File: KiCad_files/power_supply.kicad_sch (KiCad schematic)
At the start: 5 parts, among them Q2 DMP3099L, U7 LTC4412xS6

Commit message: power supply
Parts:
- removed C5: C, symbol Device:C
- added C17: 22n, symbol Device:C
- added C18, C19, C20: 0.1u, symbol Device:C
- added C21: 33p, symbol Device:C
- added C5 (x2): 22u, symbol Device:C
- added D3: 1N4148, Diode_THT:D_DO-35_SOD27_P7.62mm_Horizontal, symbol Diode:1N4148
- added L4: 5u, symbol Device:L
- added R10: 100k, symbol Device:R
- added R11: 20, symbol Device:R
- added R12: 5.6k, symbol Device:R
- added R13: 13k, symbol Device:R
- added R14: 40.2k, symbol Device:R
- added R15: 470k, symbol Device:R
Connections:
- net +3.3V: now also C21.2, C5.1, L4.2, R14.2, R15.1; no longer U8.7 (VCC)
- net GND: now also U7.3 (CTL), U8.4 (GND), C17.1, C18.1, C20.1, C5.2, C5.2, R13.1
- net VBUS: no longer U7.6 (SENSE)
- net power_mux: now also R15.2
- net at U8.1 (SS): now also C17.2
- net at D2.1 (K), Q2.2 (S), U8.2 (IN): now also U7.6 (SENSE), C20.2, C5.1, R10.2
- net at U8.3 (SW): now also C19.1, L4.1
- net at U8.5 (BST): now also D3.1 (K), R11.1
- net at U8.6 (EN/SYNC): now also R10.1
- net at U8.8 (BST): now also R12.1
- net +BATT renamed BATT
- new net: C21.1, R12.2, R13.2, R14.1
- new net: C18.2, D3.2 (A), U8.7 (VCC)
- new net: C19.2, R11.2

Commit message: sadfsadf
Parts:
- added C25, C26: 0, symbol Device:C
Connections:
- net +3.3V: now also C25.1
- net GND: now also C25.2, C26.2
- net at C20.2, C5.1, D2.1 (K)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: now also C26.1
- net BATT renamed BAT
- net power_mux renamed BAT_STAT
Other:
- note removed: "To load"
- moved on the sheet: C5

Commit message: mohloilut korjattu
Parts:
- removed C25, C26: 0, symbol Device:C
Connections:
- net BAT renamed BATT
- net BAT_STAT renamed power_mux
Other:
- note added: "To load"
- moved on the sheet: C5

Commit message: hierarkiset pinnit poweriin
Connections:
- net BATT renamed BAT
- net power_mux renamed BAT_STAT
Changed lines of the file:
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@@
+	)
+	(junction
+		(at 254 95.25)
+		(diameter 0)
+		(color 0 0 0 0)
 	)
 	(junction
@@
 	)
 	(junction
-		(at 254 118.11)
-		(diameter 0)
-		(color 0 0 0 0)
-	)
-	(junction
 		(at 152.4 72.39)
 		(diameter 0)
@@
 	)
 	(junction
-		(at 254 95.25)
+		(at 254 118.11)
 		(diameter 0)
 		(color 0 0 0 0)
@@
 	(wire
 		(pts
-			(xy 34.29 72.39) (xy 115.57 72.39)
-		)
-		(stroke
-			(width 0)
-			(type default)
-		)
-	)
-	(wire
-		(pts
 			(xy 241.3 106.68) (xy 241.3 114.3)
 		)
@@
 	(wire
 		(pts
-			(xy 34.29 85.09) (xy 58.42 85.09)
-		)
-		(stroke
-			(width 0)
-			(type default)
-		)
-	)
-	(wire
-		(pts
 			(xy 152.4 63.5) (xy 152.4 72.39)
 		)
@@
 	(wire
 		(pts
+			(xy 254 95.25) (xy 265.43 95.25)
+		)
+		(stroke
+			(width 0)
+			(type default)
+		)
+	)
+	(wire
+		(pts
 			(xy 143.51 72.39) (xy 143.51 81.28)
 		)
@@
 	(wire
 		(pts
+			(xy 109.22 72.39) (xy 115.57 72.39)
+		)
+		(stroke
+			(width 0)
+			(type default)
+		)
+	)
+	(wire
+		(pts
 			(xy 254 78.74) (xy 254 81.28)
 		)
@@
 	(wire
 		(pts
-			(xy 254 95.25) (xy 266.7 95.25)
-		)
-		(stroke
-			(width 0)
-			(type default)
-		)
-	)
-	(wire
-		(pts
 			(xy 161.29 74.93) (xy 161.29 95.25)
 		)
@@
 	(wire
 		(pts
+			(xy 254 118.11) (xy 266.7 118.11)
+		)
+		(stroke
+			(width 0)
+			(type default)
+		)
+	)
+	(wire
+		(pts
 			(xy 161.29 69.85) (xy 170.18 69.85)
 		)
@@
 	(wire
 		(pts
-			(xy 254 118.11) (xy 266.7 118.11)
+			(xy 25.4 85.09) (xy 58.42 85.09)
 		)
 		(stroke
@@
 		)
 	)
-	(global_label "power_mux"
+	(hierarchical_label "BAT"
 		(shape input)
-		(at 266.7 118.11 0)
-		(fields_autoplaced yes)
+		(at 25.4 85.09 180)
 		(effects
 			(font
 				(size 1.27 1.27)
 			)
-			(justify left)
-		)
-		(property "Intersheetrefs" "${INTERSHEET_REFS}"
-			(at 280.0265 118.11 0)
-			(show_name yes)
-			(effects
-				(font
-					(size 1.27 1.27)
-				)
-				(justify left)
-				(hide yes)
-			)
-		)
-	)
-	(global_label "VBUS"
-		(shape input)
-		(at 34.29 72.39 180)
-		(fields_autoplaced yes)
+			(justify right)
+		)
+	)
+	(hierarchical_label "BAT_STAT"
+		(shape output)
+		(at 266.7 118.11 0)
 		(effects
 			(font
 				(size 1.27 1.27)
 			)
-			(justify right)
-		)
-		(property "Intersheetrefs" "${INTERSHEET_REFS}"
-			(at 26.4062 72.39 0)
-			(effects
-				(font
-					(size 1.27 1.27)
-				)
-				(justify right)
-				(hide yes)
-			)
-		)
-	)
-	(global_label "+3.3V"
-		(shape input)
-		(at 266.7 95.25 0)
-		(fields_autoplaced yes)
-		(effects
-			(font
-				(size 1.27 1.27)
-			)
 			(justify left)
-		)
-		(property "Intersheetrefs" "${INTERSHEET_REFS}"
-			(at 275.37 95.25 0)
-			(effects
-				(font
-					(size 1.27 1.27)
-				)
-				(justify left)
-				(hide yes)
-			)
-		)
-	)
-	(global_label "BATT"
-		(shape input)
-		(at 34.29 85.09 180)
-		(fields_autoplaced yes)
-		(effects
-			(font
-				(size 1.27 1.27)
-			)
-			(justify right)
-		)
-		(property "Intersheetrefs" "${INTERSHEET_REFS}"
-			(at 27.011 85.09 0)
-			(effects
-				(font
-					(size 1.27 1.27)
-				)
-				(justify right)
-				(hide yes)
-			)
 		)
 	)
@@
 	)
 	(symbol
+		(lib_id "power:VBUS")
+		(at 109.22 72.39 90)
+		(unit 1)
+		(exclude_from_sim no)
+		(in_bom yes)
+		(on_board yes)
+		(dnp no)
+		(fields_autoplaced yes)
+		(property "Reference" "#PWR021"
+			(at 113.03 72.39 0)
+			(effects
+				(font
+					(size 1.27 1.27)
+				)
+				(hide yes)
+			)
+		)
+		(property "Value" "VBUS"
+			(at 105.41 72.3899 90)
+			(effects
+				(font
+					(size 1.27 1.27)
+				)
+				(justify left)
+			)
+		)
+		(property "Footprint" ""
+			(at 109.22 72.39 0)
+			(effects
+				(font
+					(size 1.27 1.27)
+				)
+				(hide yes)
+			)
+		)
+		(property "Datasheet" ""
+			(at 109.22 72.39 0)
+			(effects
+				(font
+					(size 1.27 1.27)
+				)
+				(hide yes)
+			)
+		)
+		(property "Description" "Power symbol creates a global label with name \"VBUS\""
+			(at 109.22 72.39 0)
+			(effects
+				(font
+					(size 1.27 1.27)
+				)
+				(hide yes)
+			)
+		)
+		(pin "1"
+		)
+		(instances
+			(project ""
+				(path "/186d5500-054c-4b47-a89c-85f6ce2abe33/718dca9f-314d-4628-afec-7956f3606013"
+					(reference "#PWR021")
+					(unit 1)
+				)
+			)
+		)
+	)
+	(symbol
 		(lib_id "Device:R")
 		(at 214.63 69.85 90)
@@
 					(unit 1)
 				)
+			)
+		)
+	)
+	(symbol
+		(lib_id "power:+3.3V")
+		(at 265.43 95.25 270)
+		(unit 1)
+		(exclude_from_sim no)
+		(in_bom yes)
+		(on_board yes)
+		(dnp no)
+		(fields_autoplaced yes)
+		(property "Reference" "#PWR020"
+			(at 261.62 95.25 0)
+			(effects
+				(font
+					(size 1.27 1.27)
+				)
+				(hide yes)
+			)
+		)
+		(property "Value" "+3.3V"
+			(at 269.24 95.2499 90)
+			(effects
+				(font
+					(size 1.27 1.27)
+				)
+				(justify left)
+			)
+		)
+		(property "Footprint" ""
+			(at 265.43 95.25 0)
+			(effects
+				(font
+					(size 1.27 1.27)
+				)
+				(hide yes)
+			)
+		)
+		(property "Datasheet" ""
+			(at 265.43 95.25 0)
+			(effects
+				(font
+					(size 1.27 1.27)
+				)
+				(hide yes)
+			)
+		)
+		(property "Description" "Power symbol creates a global label with name \"+3.3V\""
+			(at 265.43 95.25 0)
+			(effects
+				(font
+					(size 1.27 1.27)
+				)
+				(hide yes)
+			)
+		)
+		(pin "1"
+		)
+		(instances
+			(project ""
+				(path "/186d5500-054c-4b47-a89c-85f6ce2abe33/718dca9f-314d-4628-afec-7956f3606013"
+					(reference "#PWR020")
+					(unit 1)
+				)

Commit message: tekstiä
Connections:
- net BAT renamed BATT
- net BAT_STAT renamed power_mux

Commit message: footprinttejä
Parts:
- added C25, C26: 0, symbol Device:C
- U8: footprint (none) -> Package_TO_SOT_SMD:TSOT-23-8
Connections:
- net +3.3V: now also C25.1
- net GND: now also C25.2, C26.2
- net at C20.2, C5.1, D2.1 (K)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: now also C26.1
- net BATT renamed BAT
- net power_mux renamed BAT_STAT
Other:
- note removed: "To load"
- moved on the sheet: C5

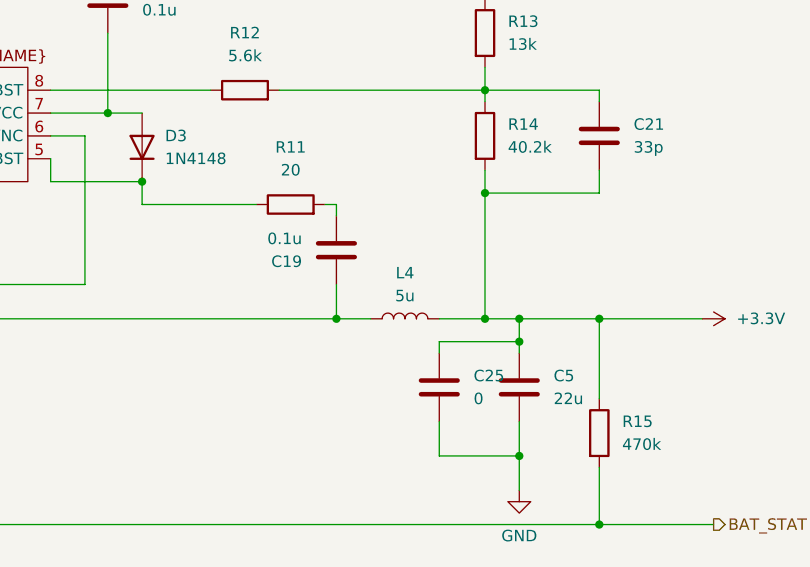
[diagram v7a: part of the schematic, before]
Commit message: footprints for powersupply
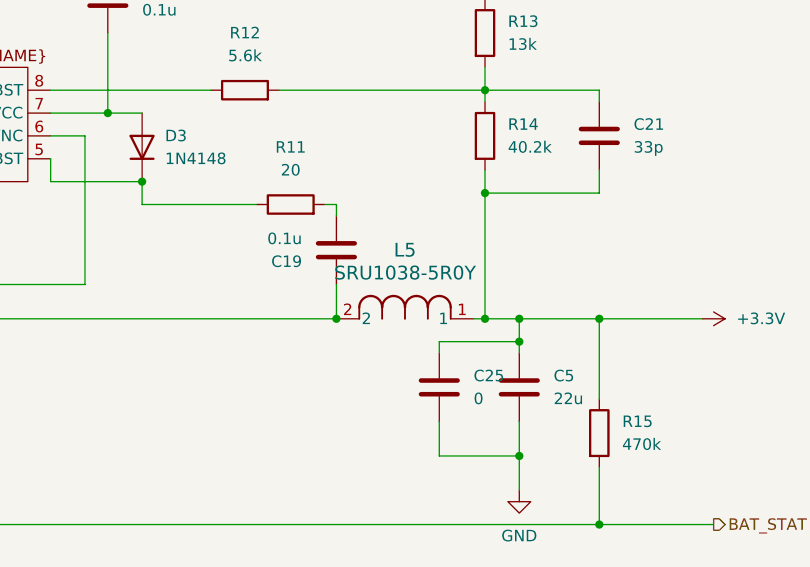
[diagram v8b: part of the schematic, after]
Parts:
- removed L4: 5u, symbol Device:L
- added L5: SRU1038-5R0Y, Inductor_SMD:L_Bourns-SRU1028_10.0x10.0mm, symbol 1_projektin osat:SRU1038-5R0Y
- C17, C18, C19, C20, C21: footprint (none) -> Capacitor_SMD:C_0805_2012Metric_Pad1.18x1.45mm_HandSolder
- C25, C26, C5: footprint (none) -> Capacitor_SMD:C_1206_3216Metric_Pad1.33x1.80mm_HandSolder
- D2: footprint (none) -> Diode_SMD:D_SOD-323_HandSoldering
- D3: footprint Diode_THT:D_DO-35_SOD27_P7.62mm_Horizontal -> Diode_SMD:D_SOD-323F
- R10, R11, R12, R13, R14, R15: footprint (none) -> Resistor_SMD:R_0805_2012Metric_Pad1.20x1.40mm_HandSolder
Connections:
- net +3.3V: now also L5.1
- net at C19.1, U8.3 (SW): now also L5.2
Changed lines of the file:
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@@
+	)
+	(junction
+		(at 142.24 90.17)
+		(diameter 0)
+		(color 0 0 0 0)
 	)
 	(junction
@@
 	)
 	(junction
-		(at 142.24 90.17)
+		(at 245.11 95.25)
+		(diameter 0)
+		(color 0 0 0 0)
+	)
+	(junction
+		(at 125.73 72.39)
+		(diameter 0)
+		(color 0 0 0 0)
+	)
+	(junction
+		(at 142.24 77.47)
+		(diameter 0)
+		(color 0 0 0 0)
+	)
+	(junction
+		(at 152.4 72.39)
+		(diameter 0)
+		(color 0 0 0 0)
+	)
+	(junction
+		(at 241.3 81.28)
+		(diameter 0)
+		(color 0 0 0 0)
+	)
+	(junction
+		(at 80.01 128.27)
+		(diameter 0)
+		(color 0 0 0 0)
+	)
+	(junction
+		(at 241.3 69.85)
+		(diameter 0)
+		(color 0 0 0 0)
+	)
+	(junction
+		(at 245.11 110.49)
 		(diameter 0)
 		(color 0 0 0 0)
@@
 	)
 	(junction
-		(at 245.11 95.25)
-		(diameter 0)
-		(color 0 0 0 0)
-	)
-	(junction
-		(at 125.73 72.39)
-		(diameter 0)
-		(color 0 0 0 0)
-	)
-	(junction
-		(at 142.24 77.47)
-		(diameter 0)
-		(color 0 0 0 0)
-	)
-	(junction
-		(at 152.4 72.39)
-		(diameter 0)
-		(color 0 0 0 0)
-	)
-	(junction
-		(at 241.3 81.28)
-		(diameter 0)
-		(color 0 0 0 0)
-	)
-	(junction
-		(at 80.01 128.27)
-		(diameter 0)
-		(color 0 0 0 0)
-	)
-	(junction
-		(at 241.3 69.85)
-		(diameter 0)
-		(color 0 0 0 0)
-	)
-	(junction
-		(at 245.11 110.49)
-		(diameter 0)
-		(color 0 0 0 0)
-	)
-	(junction
 		(at 203.2 80.01)
 		(diameter 0)
@@
 	(wire
 		(pts
-			(xy 236.22 95.25) (xy 241.3 95.25)
-		)
-		(stroke
-			(width 0)
-			(type default)
-		)
-	)
-	(wire
-		(pts
 			(xy 245.11 95.25) (xy 254 95.25)
 		)
@@
 	(wire
 		(pts
-			(xy 224.79 95.25) (xy 228.6 95.25)
-		)
-		(stroke
-			(width 0)
-			(type default)
-		)
-	)
-	(wire
-		(pts
 			(xy 109.22 72.39) (xy 115.57 72.39)
 		)
@@
 		(pts
 			(xy 161.29 69.85) (xy 170.18 69.85)
+		)
+		(stroke
+			(width 0)
+			(type default)
+		)
+	)
+	(wire
+		(pts
+			(xy 240.03 95.25) (xy 241.3 95.25)
 		)
 		(stroke
@@
 			)
 		)
-		(property "Footprint" ""
+		(property "Footprint" "Capacitor_SMD:C_0805_2012Metric_Pad1.18x1.45mm_HandSolder"
 			(at 153.3652 63.5 0)
 			(effects
@@
 			)
 		)
-		(property "Footprint" ""
+		(property "Footprint" "Capacitor_SMD:C_0805_2012Metric_Pad1.18x1.45mm_HandSolder"
 			(at 254.9652 78.74 0)
 			(effects
@@
 			)
 		)
-		(property "Footprint" ""
+		(property "Footprint" "Capacitor_SMD:C_0805_2012Metric_Pad1.18x1.45mm_HandSolder"
 			(at 162.2552 63.5 0)
 			(effects
@@
 			)
 		)
-		(property "Footprint" ""
+		(property "Footprint" "Resistor_SMD:R_0805_2012Metric_Pad1.20x1.40mm_HandSolder"
 			(at 252.222 107.95 90)
 			(effects
@@
 	)
 	(symbol
+		(lib_id "1_projektin osat:SRU1038-5R0Y")
+		(at 224.79 95.25 0)
+		(unit 1)
+		(exclude_from_sim no)
+		(in_bom yes)
+		(on_board yes)
+		(dnp no)
+		(fields_autoplaced yes)
+		(property "Reference" "L5"
+			(at 232.41 87.63 0)
+			(effects
+				(font
+					(size 1.524 1.524)
+				)
+			)
+		)
+		(property "Value" "SRU1038-5R0Y"
+			(at 232.41 90.17 0)
+			(effects
+				(font
+					(size 1.524 1.524)
+				)
+			)
+		)
+		(property "Footprint" "Inductor_SMD:L_Bourns-SRU1028_10.0x10.0mm"
+			(at 224.79 95.25 0)
+			(effects
+				(font
+					(size 1.27 1.27)
+					(italic yes)
+				)
+				(hide yes)
+			)
+		)
+		(property "Datasheet" "SRU1038-5R0Y"
+			(at 224.79 95.25 0)
+			(effects
+				(font
+					(size 1.27 1.27)
+					(italic yes)
+				)
+				(hide yes)
+			)
+		)
+		(property "Description" ""
+			(at 224.79 95.25 0)
+			(effects
+				(font
+					(size 1.27 1.27)
+				)
+				(hide yes)
+			)
+		)
+		(pin "2"
+		)
+		(pin "1"
+		)
+		(instances
+			(project ""
+				(path "/186d5500-054c-4b47-a89c-85f6ce2abe33/718dca9f-314d-4628-afec-7956f3606013"
+					(reference "L5")
+					(unit 1)
+				)
+			)
+		)
+	)
+	(symbol
 		(lib_id "Device:R")
 		(at 241.3 74.93 0)
@@
 			)
 		)
-		(property "Footprint" ""
+		(property "Footprint" "Resistor_SMD:R_0805_2012Metric_Pad1.20x1.40mm_HandSolder"
 			(at 239.522 74.93 90)
 			(effects
@@
 			)
 		)
-		(property "Footprint" ""
+		(property "Footprint" "Capacitor_SMD:C_0805_2012Metric_Pad1.18x1.45mm_HandSolder"
 			(at 200.3552 63.5 0)
 			(effects
@@
 			)
 		)
-		(property "Footprint" ""
+		(property "Footprint" "Capacitor_SMD:C_1206_3216Metric_Pad1.33x1.80mm_HandSolder"
 			(at 237.1852 106.68 0)
 			(effects
@@
 			)
 		)
-		(property "Footprint" ""
+		(property "Footprint" "Capacitor_SMD:C_1206_3216Metric_Pad1.33x1.80mm_HandSolder"
 			(at 246.0752 106.68 0)
 			(effects
@@
 			)
 		)
-		(property "Footprint" ""
+		(property "Footprint" "Resistor_SMD:R_0805_2012Metric_Pad1.20x1.40mm_HandSolder"
 			(at 239.522 63.5 90)
 			(effects
@@
 			)
 		)
-		(property "Footprint" ""
+		(property "Footprint" "Diode_SMD:D_SOD-323_HandSoldering"
 			(at 119.38 72.39 0)
 			(effects
@@
 			)
 		)
-		(property "Footprint" ""
+		(property "Footprint" "Capacitor_SMD:C_1206_3216Metric_Pad1.33x1.80mm_HandSolder"
 			(at 143.2052 88.9 0)
 			(effects
@@
 			)
 		)
-		(property "Footprint" "Diode_THT:D_DO-35_SOD27_P7.62mm_Horizontal"
+		(property "Footprint" "Diode_SMD:D_SOD-323F"
 			(at 203.2 76.2 0)
 			(effects
@@
 			)
 		)
-		(property "Footprint" ""
+		(property "Footprint" "Resistor_SMD:R_0805_2012Metric_Pad1.20x1.40mm_HandSolder"
 			(at 219.71 84.328 90)
 			(effects
@@
 			)
 		)
-		(property "Footprint" ""
+		(property "Footprint" "Capacitor_SMD:C_1206_3216Metric_Pad1.33x1.80mm_HandSolder"
 			(at 133.0452 88.9 0)
 			(effects
@@
 			)
 		)
-		(property "Footprint" ""
+		(property "Footprint" "Resistor_SMD:R_0805_2012Metric_Pad1.20x1.40mm_HandSolder"
 			(at 214.63 71.628 90)
 			(effects
@@
 	)
 	(symbol
-		(lib_id "Device:L")
-		(at 232.41 95.25 90)
-		(unit 1)
-		(exclude_from_sim no)
-		(in_bom yes)
-		(on_board yes)
-		(dnp no)
-		(property "Reference" "L4"
-			(at 232.41 90.17 90)
-			(effects
-				(font
-					(size 1.27 1.27)
-				)
-			)
-		)
-		(property "Value" "5u"
-			(at 232.41 92.71 90)
-			(effects
-				(font
-					(size 1.27 1.27)
-				)
-			)
-		)
-		(property "Footprint" ""
-			(at 232.41 95.25 0)
-			(effects
-				(font
-					(size 1.27 1.27)
-				)
-				(hide yes)
-			)
-		)
-		(property "Datasheet" "~"
-			(at 232.41 95.25 0)
-			(effects
-				(font
-					(size 1.27 1.27)
-				)
-				(hide yes)
-			)
-		)
-		(property "Description" "Inductor"
-			(at 232.41 95.25 0)
-			(effects
-				(font
-					(size 1.27 1.27)
-				)
-				(hide yes)
-			)
-		)
-		(pin "2"
-		)
-		(pin "1"
-		)
-		(instances
-			(project "esp"
-				(path "/186d5500-054c-4b47-a89c-85f6ce2abe33/718dca9f-314d-4628-afec-7956f3606013"
-					(reference "L4")
-					(unit 1)
-				)
-			)
-		)
-	)
-	(symbol
 		(lib_id "power:GND")
 		(at 80.01 130.81 0)
@@
 			)
 		)
-		(property "Footprint" ""
+		(property "Footprint" "Capacitor_SMD:C_0805_2012Metric_Pad1.18x1.45mm_HandSolder"
 			(at 223.8248 83.82 0)
 			(effects
@@
 			)
 		)
-		(property "Footprint" ""
+		(property "Footprint" "Resistor_SMD:R_0805_2012Metric_Pad1.20x1.40mm_HandSolder"
 			(at 154.178 85.09 90)
 			(effects
